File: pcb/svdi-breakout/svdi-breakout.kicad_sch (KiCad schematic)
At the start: 2 parts, among them J1 FPC31, J2 HDR40

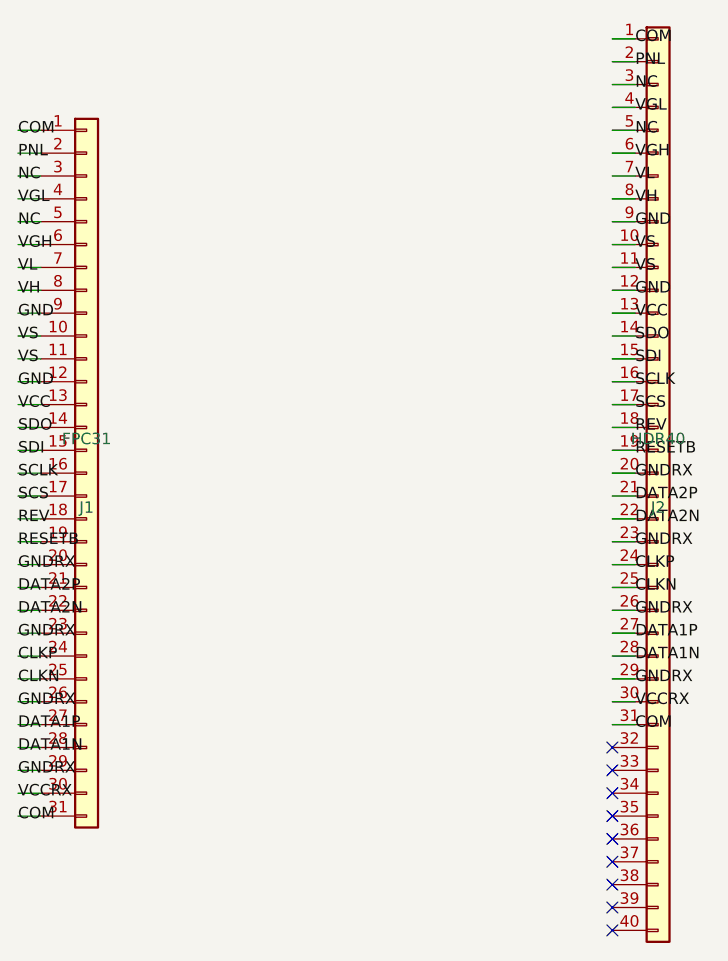
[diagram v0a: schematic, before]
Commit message: Phase 4: SVDI breakout PCB, DRC clean through full verify gate
- scripts/gen_svdi_breakout_pcb.py: deterministic headless pcbnew generator
  (netlist-driven pad-net binding, board outline, GND pour)
- Routing v5 (layer-split switchbox): F.Cu vertical stubs per J1 pad (0.5 mm
  pitch, via1 0.35/0.2 at y=41.5), B.Cu verticals to stepped rows via2,
  F.Cu horizontals at each net's J2 pad row landing on the plated pad, and
  F.Cu upper ties for multi-pin nets (COM/NC/VS) with span-ordered stagger
  (widest span highest) so no tie crosses another net's stub
- Geometry verified against DRC iteratively; constraints for this bench
  board written to board.design_settings.rules in the project file
  (via 0.35/0.2, clearance 0.13, hole_clearance 0.15, hole_to_hole 0.2)
- Gate results: ERC 0 violations, DRC 0 violations, 0 unconnected pads,
  STEP export OK (board+J2; J1 3D model unavailable in KiCad library,
  documented as U9 in docs/UNKNOWNS.md). Mechanical check BLOCKED as
  designed until a measured enclosure solid exists (no fake geometry).
- verify-design.sh: exit 3 = BLOCKED branch, as intended
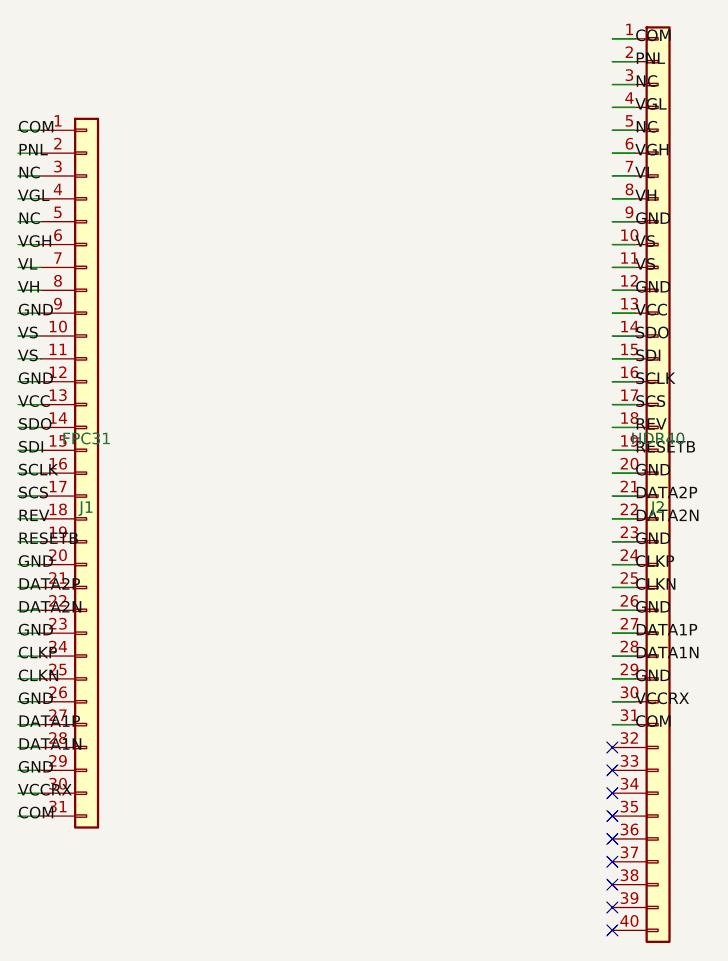
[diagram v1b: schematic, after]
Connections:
- net GNDRX is gone; now on net GND: J1.20 (Pin_20), J1.23 (Pin_23), J1.26 (Pin_26), J1.29 (Pin_29), J2.20 (Pin_20), J2.23 (Pin_23), J2.26 (Pin_26), J2.29 (Pin_29)
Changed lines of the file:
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@@
 		(effects (font (size 1.27 1.27)))
 	)
-	(label "GNDRX"
+	(label "GND"
 		(at 119.38 86.36 0)
 		(effects (font (size 1.27 1.27)))
@@
 		(effects (font (size 1.27 1.27)))
 	)
-	(label "GNDRX"
+	(label "GND"
 		(at 119.38 93.98 0)
 		(effects (font (size 1.27 1.27)))
@@
 		(effects (font (size 1.27 1.27)))
 	)
-	(label "GNDRX"
+	(label "GND"
 		(at 119.38 101.60 0)
 		(effects (font (size 1.27 1.27)))
@@
 		(effects (font (size 1.27 1.27)))
 	)
-	(label "GNDRX"
+	(label "GND"
 		(at 119.38 109.22 0)
 		(effects (font (size 1.27 1.27)))
@@
 		(effects (font (size 1.27 1.27)))
 	)
-	(label "GNDRX"
+	(label "GND"
 		(at 187.96 76.20 0)
 		(effects (font (size 1.27 1.27)))
@@
 		(effects (font (size 1.27 1.27)))
 	)
-	(label "GNDRX"
+	(label "GND"
 		(at 187.96 83.82 0)
 		(effects (font (size 1.27 1.27)))
@@
 		(effects (font (size 1.27 1.27)))
 	)
-	(label "GNDRX"
+	(label "GND"
 		(at 187.96 91.44 0)
 		(effects (font (size 1.27 1.27)))
@@
 		(effects (font (size 1.27 1.27)))
 	)
-	(label "GNDRX"
+	(label "GND"
 		(at 187.96 99.06 0)
 		(effects (font (size 1.27 1.27)))
